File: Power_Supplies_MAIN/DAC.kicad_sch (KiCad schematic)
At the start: 51 parts, among them J1 Line Out (Left), J2 Headphone Out, J21 Line Out (Right), J33 PINHD_1x3_Female, J36 PINHD_1x2_Female, U10 OPA2134, U11 TPA6110A2DGN, U34 NE5532AD, U35 NE5532AD, U9 PCM1780

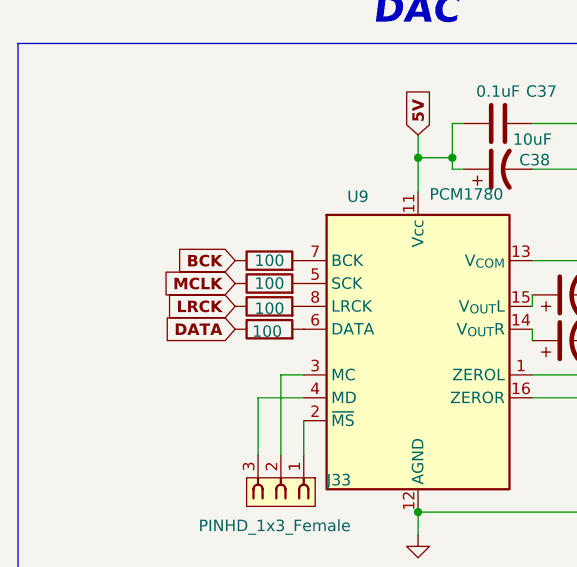
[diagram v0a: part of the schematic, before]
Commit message: updated main PCB to reflect changes w/ new mcu
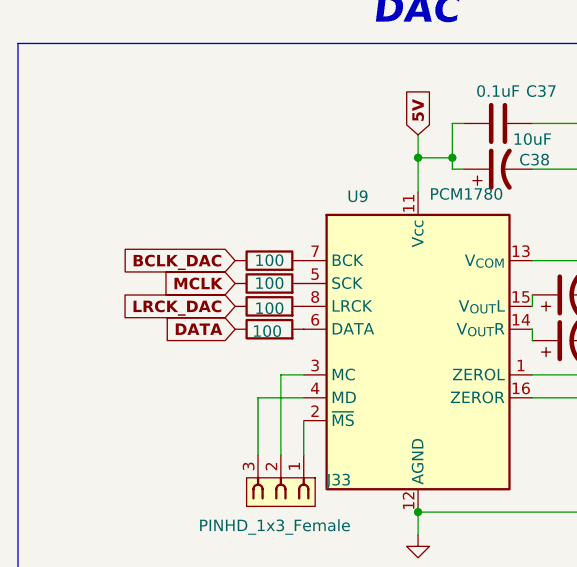
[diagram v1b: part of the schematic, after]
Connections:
- net BCK renamed BCLK_DAC
- net LRCK renamed LRCK_DAC
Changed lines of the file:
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@@
 		)
 	)
-	(global_label "BCK"
+	(global_label "BCLK_DAC"
 		(shape input)
 		(at 39.37 43.18 180)
@@
 		)
 		(property "Intersheetrefs" "${INTERSHEET_REFS}"
-			(at 32.0988 43.18 0)
+			(at 26.4745 43.18 0)
 			(effects
 				(font
@@
 		)
 	)
-	(global_label "LRCK"
+	(global_label "LRCK_DAC"
 		(shape input)
 		(at 39.37 48.26 180)
@@
 		)
 		(property "Intersheetrefs" "${INTERSHEET_REFS}"
-			(at 31.0707 48.26 0)
+			(at 26.4745 48.26 0)
 			(effects
 				(font

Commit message: fixed a lot of stuff
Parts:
- removed C31, C32: 1200pF, Capacitor_SMD:C_0603_1608Metric_Pad1.08x0.95mm_HandSolder, symbol Device:C
- removed C33, C35: 120pF, Capacitor_SMD:C_0603_1608Metric_Pad1.08x0.95mm_HandSolder, symbol Device:C
- removed C47: 10uF, Capacitor_SMD:C_0805_2012Metric, symbol Device:C
- removed J33: PINHD_1x3_Female, Connector_PinSocket_2.54mm:PinSocket_1x03_P2.54mm_Vertical, symbol PCM_SL_Pin_Headers:PINHD_1x3_Female
- removed J36: PINHD_1x2_Female, Connector_PinSocket_2.54mm:PinSocket_1x02_P2.54mm_Vertical, symbol PCM_SL_Pin_Headers:PINHD_1x2_Female
- added C9: 10uF, Capacitor_SMD:CP_Elec_4x5.8, symbol Device:C_Polarized_US
- added D5, D6: LED, LED_SMD:LED_0402_1005Metric_Pad0.77x0.64mm_HandSolder, symbol PCM_SL_Devices:LED
- added J12: PINHD_1x3_Male, Connector_PinHeader_2.54mm:PinHeader_1x03_P2.54mm_Vertical, symbol PCM_SL_Pin_Headers:PINHD_1x3_Male
- added J15: PINHD_1x2_Male, Connector_PinHeader_2.54mm:PinHeader_1x02_P2.54mm_Vertical, symbol PCM_SL_Pin_Headers:PINHD_1x2_Male
- added R13, R14: 2.2k, Resistor_SMD:R_0805_2012Metric, symbol Device:R
- J1, J2, J21: footprint Connector_Audio:Jack_3.5mm_CUI_SJ-3523-SMT_Horizontal -> SamacSys_Parts:ACJSNV353
- R19, R21, R22: value 100 -> 50
- R20: value 100 -> 0R
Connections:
- net 5V: now also C9.1, D5.2, D6.2
- net AGND: now also J1.1, J2.1, J21.1, C9.2, R13.2, R14.2; no longer J1.S, J2.S, J21.S
- net LEFT_OUT: now also J2.3; no longer J2.T
- net LEFT_OUT+: now also J1.4; no longer J1.R
- net LEFT_OUT-: now also J1.3; no longer J1.T
- net RIGHT_OUT: now also J2.4; no longer J2.R
- net RIGHT_OUT+: now also J21.4; no longer J21.R
- net RIGHT_OUT-: now also J21.3; no longer J21.T
- net at U9.2 (~{MS}): now also J12.1
- net at U9.3 (MC): now also J12.2
- net at U9.4 (MD): now also J12.3
- net at U9.1 (ZEROL): now also J15.1
- net at U9.16 (ZEROR): now also J15.2
- new net: D5.1, R13.1
- new net: D6.1, R14.1
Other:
- moved on the sheet: R32
